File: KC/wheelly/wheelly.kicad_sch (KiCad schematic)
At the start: 28 parts, among them M2 Motor_Servo_Grapner_JR, P1 Power, P2 Analog, P3 Digital, P4 Digital, P5 CONN_01X01, P6 CONN_01X01, P7 CONN_01X01, P8 CONN_01X01, U1 74HC595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

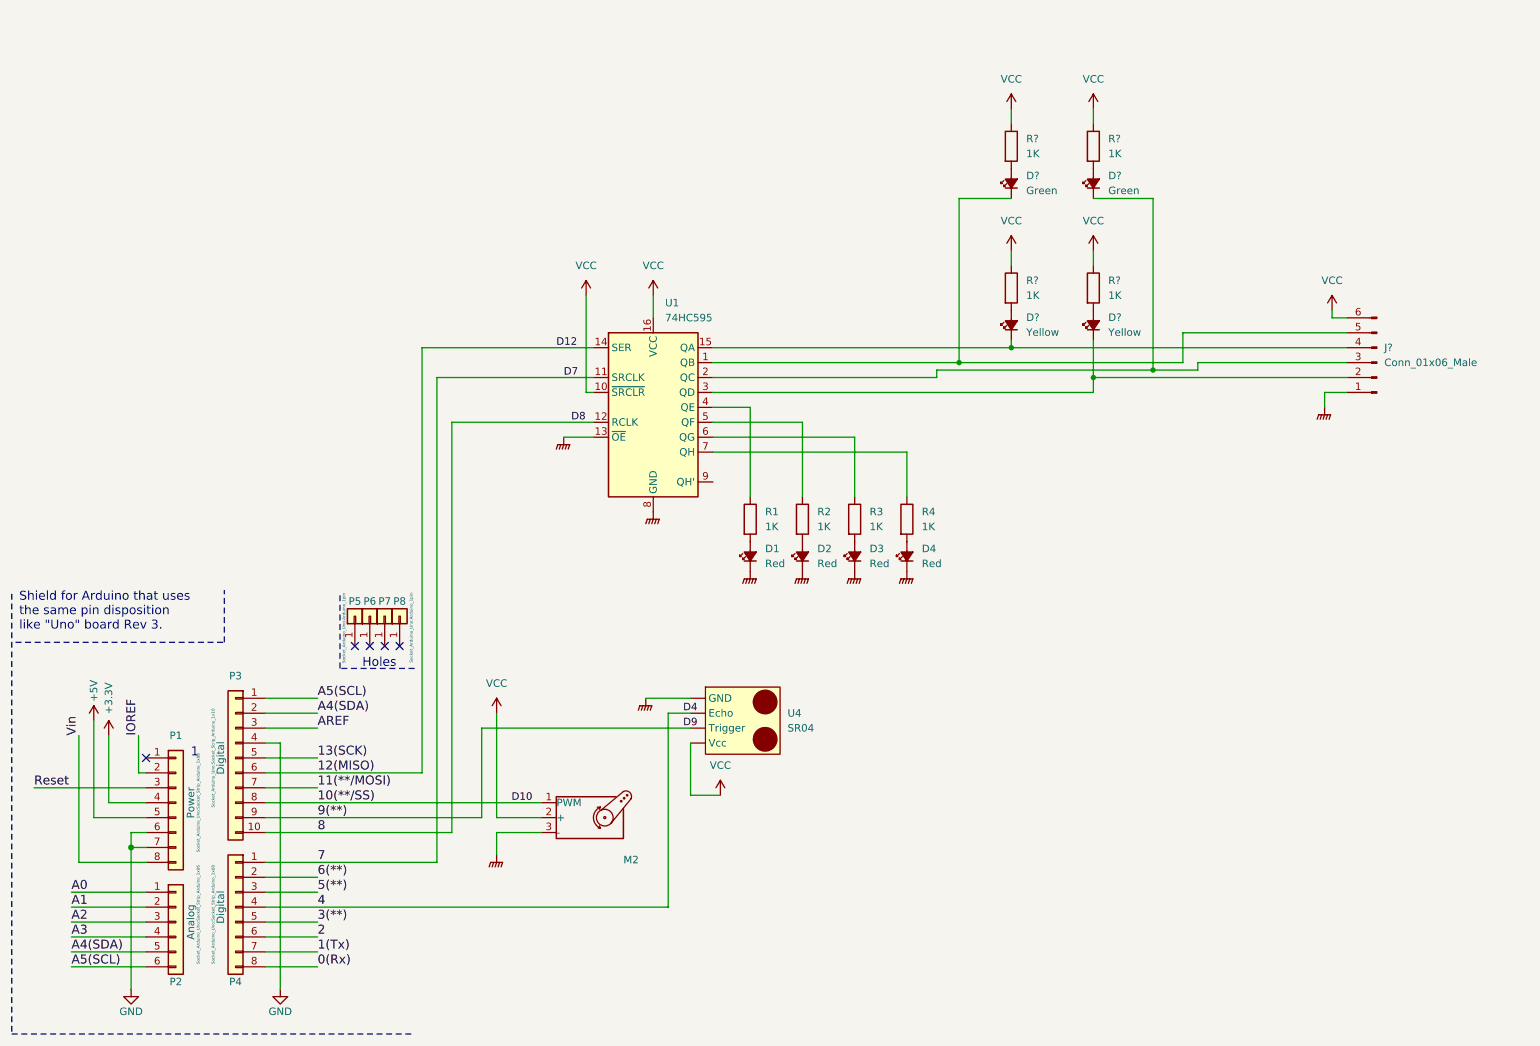
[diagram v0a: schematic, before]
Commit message: remove shift latch
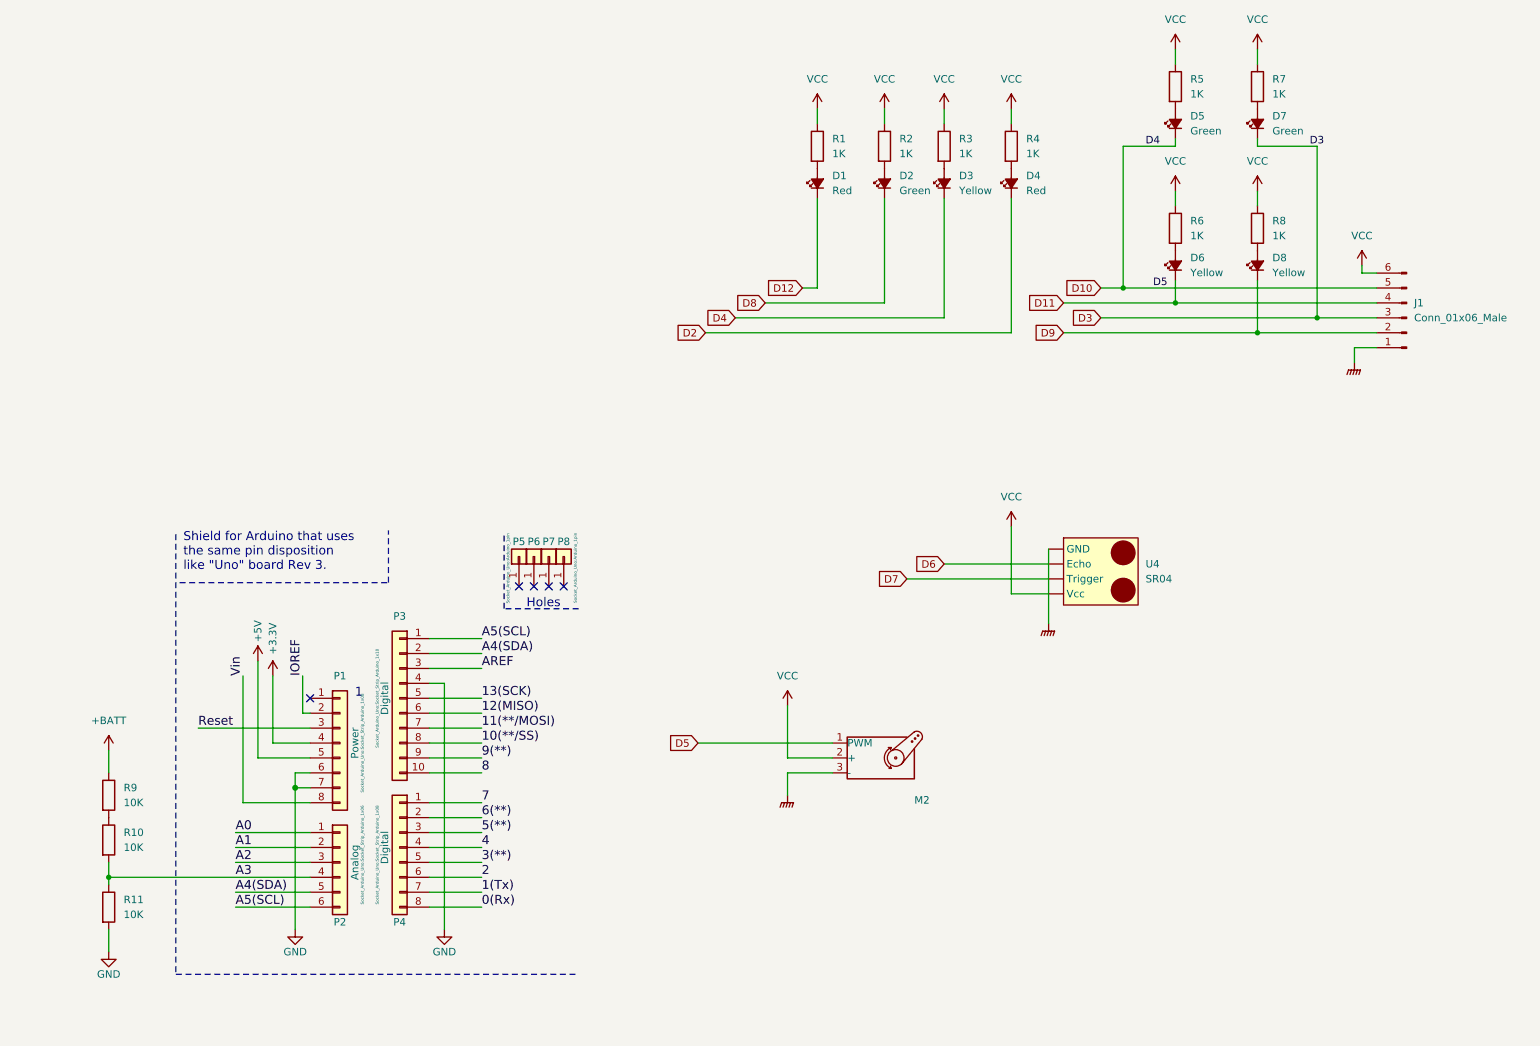
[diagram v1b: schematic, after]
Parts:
- removed U1: 74HC595, symbol 74xx:74HC595
- added R10, R11, R9: 10K, symbol Device:R
- D2: value Red -> Green
- D3: value Red -> Yellow
- gave numbers to parts that had none: 9
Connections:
- net 10(**/SS): no longer M2.1 (PWM)
- net 4: no longer U4. (Vcc)
- net 9(**): no longer U4. (Vcc)
- net A3: now also R10.2, R11.1
- net GND: now also R11.2
- net GNDPWR: no longer D1.1 (K), D2.1 (K), D3.1 (K), D4.1 (K)
- net VCC: now also R1.1, R2.1, R3.1, R4.1
- net D10: now reaches D5.1 (K), J1.5 (Pin_5)
- net D10: now also D3.1 (K), M2.1 (PWM)
- net D9: now reaches D8.1 (K), J1.2 (Pin_2)
- net D11: now reaches D6.1 (K), J1.4 (Pin_4)
- net D3: now reaches D7.1 (K), J1.3 (Pin_3)
- new net: R10.1, R9.2
- new net +BATT: R9.1
- new net D12: D1.1 (K)
- new net D2: D4.1 (K)
- new net D6: U4. (Vcc)
- new net D7: U4. (Vcc)
- new net D8: D2.1 (K)
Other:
- moved on the sheet: D1, D2, D3, D4, D5, D6, D7, D8, J1, M2, P1, P2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

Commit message: Add gyroscope and accelerometer for motion traking #11
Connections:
- net D10: now also D4.1 (K); no longer D3.1 (K), D5.1 (K), J1.5 (Pin_5), M2.1 (PWM)
- net D11: now also D5.1 (K), D8.1 (K), J1.2 (Pin_2), J1.5 (Pin_5); no longer D6.1 (K), J1.4 (Pin_4)
- net D2: now also D2.1 (K); no longer D4.1 (K)
- net D6: now also D6.1 (K), J1.4 (Pin_4); no longer U4. (Vcc)
- net D8: now also U4. (Vcc); no longer D2.1 (K)
- net D9: now also M2.1 (PWM); no longer D8.1 (K), J1.2 (Pin_2)
- new net D4: D3.1 (K)
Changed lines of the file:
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@@
     (effects (font (size 1.524 1.524)) (justify left bottom))
-  )
-  (label "D3" (at 242.57 44.45 0)
-    (effects (font (size 1.27 1.27)) (justify left bottom))
   )
   (label "0(Rx)" (at 101.6 173.99 0)
@@
     (effects (font (size 1.524 1.524)) (justify left bottom))
   )
-  (label "D4" (at 214.63 44.45 0)
-    (effects (font (size 1.27 1.27)) (justify left bottom))
-  )
   (label "7" (at 101.6 156.21 0)
     (effects (font (size 1.524 1.524)) (justify left bottom))
@@
     (effects (font (size 1.524 1.524)) (justify left bottom))
   )
-  (global_label "D8" (shape input) (at 149.86 71.12 180) (fields_autoplaced)
+  (global_label "D2" (shape input) (at 149.86 71.12 180) (fields_autoplaced)
     (effects (font (size 1.27 1.27)) (justify right))
     (property "Intersheet References" "${INTERSHEET_REFS}" (id 0) (at 144.7769 71.0406 0)
@@
     )
   )
-  (global_label "D7" (shape input) (at 173.99 118.11 180) (fields_autoplaced)
+  (global_label "D8" (shape input) (at 173.99 118.11 180) (fields_autoplaced)
     (effects (font (size 1.27 1.27)) (justify right))
     (property "Intersheet References" "${INTERSHEET_REFS}" (id 0) (at 168.9069 118.0306 0)
@@
     )
   )
-  (global_label "D5" (shape input) (at 138.43 146.05 180) (fields_autoplaced)
+  (global_label "D9" (shape input) (at 138.43 146.05 180) (fields_autoplaced)
     (effects (font (size 1.27 1.27)) (justify right))
     (property "Intersheet References" "${INTERSHEET_REFS}" (id 0) (at 133.3469 145.9706 0)
@@
     )
   )
-  (global_label "D2" (shape input) (at 139.7 76.2 180) (fields_autoplaced)
-    (effects (font (size 1.27 1.27)) (justify right))
-    (property "Intersheet References" "${INTERSHEET_REFS}" (id 0) (at 134.6169 76.1206 0)
-      (effects (font (size 1.27 1.27)) (justify right) hide)
-    )
-  )
-  (global_label "D6" (shape input) (at 180.34 115.57 180) (fields_autoplaced)
+  (global_label "D10" (shape input) (at 139.7 76.2 180) (fields_autoplaced)
+    (effects (font (size 1.27 1.27)) (justify right))
+    (property "Intersheet References" "${INTERSHEET_REFS}" (id 0) (at 133.4074 76.1206 0)
+      (effects (font (size 1.27 1.27)) (justify right) hide)
+    )
+  )
+  (global_label "D7" (shape input) (at 180.34 115.57 180) (fields_autoplaced)
     (effects (font (size 1.27 1.27)) (justify right))
     (property "Intersheet References" "${INTERSHEET_REFS}" (id 0) (at 175.2569 115.4906 0)
@@
     )
   )
-  (global_label "D10" (shape input) (at 207.01 68.58 180) (fields_autoplaced)
+  (global_label "D11" (shape input) (at 207.01 68.58 180) (fields_autoplaced)
     (effects (font (size 1.27 1.27)) (justify right))
     (property "Intersheet References" "${INTERSHEET_REFS}" (id 0) (at 200.7174 68.5006 0)
@@
     )
   )
-  (global_label "D9" (shape input) (at 200.66 76.2 180) (fields_autoplaced)
+  (global_label "D5" (shape input) (at 200.66 76.2 180) (fields_autoplaced)
     (effects (font (size 1.27 1.27)) (justify right))
     (property "Intersheet References" "${INTERSHEET_REFS}" (id 0) (at 195.5769 76.1206 0)
@@
     )
   )
-  (global_label "D11" (shape input) (at 200.66 71.12 180) (fields_autoplaced)
-    (effects (font (size 1.27 1.27)) (justify right))
-    (property "Intersheet References" "${INTERSHEET_REFS}" (id 0) (at 194.3674 71.0406 0)
+  (global_label "D6" (shape input) (at 200.66 71.12 180) (fields_autoplaced)
+    (effects (font (size 1.27 1.27)) (justify right))
+    (property "Intersheet References" "${INTERSHEET_REFS}" (id 0) (at 195.5769 71.0406 0)
       (effects (font (size 1.27 1.27)) (justify right) hide)
     )
@@
   (symbol (lib_id "power:+BATT") (at 38.1 147.32 0) (unit 1)
     (in_bom yes) (on_board yes) (fields_autoplaced)
-    (property "Reference" "#PWR?" (id 0) (at 38.1 151.13 0)
+    (property "Reference" "#PWR018" (id 0) (at 38.1 151.13 0)
       (effects (font (size 1.27 1.27)) hide)
     )
@@
       (reference "#PWR017") (unit 1) (value "GND") (footprint "")
     )
+    (path "/1fb34dd7-9347-4cf4-b810-dadeb7c77811"
+      (reference "#PWR018") (unit 1) (value "+BATT") (footprint "")
+    )
     (path "/c8fbf131-b7fa-4c09-b6b1-aafb3230f181"
       (reference "#PWR0103") (unit 1) (value "VCC") (footprint "")
@@
       (reference "#PWR0104") (unit 1) (value "GNDPWR") (footprint "")
     )
-    (path "/1fb34dd7-9347-4cf4-b810-dadeb7c77811"
-      (reference "#PWR?") (unit 1) (value "+BATT") (footprint "")
-    )
     (path "/4dc0181e-1638-4068-9c34-c740e59b984b"
